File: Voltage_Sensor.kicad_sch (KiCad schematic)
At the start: 48 parts, among them IC1 AMC1350DWVR, IC2 AMC1350DWVR, U1 TLV9002QDRQ1, U2 TLV9002QDRQ1

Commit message: saving
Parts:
- removed C17: 1uF, Capacitor_SMD:C_0603_1608Metric_Pad1.08x0.95mm_HandSolder, symbol Device:C
- removed U2: TLV9002QDRQ1, Package_SO:SOIC-8_3.9x4.9mm_P1.27mm, symbol UTSVT-Misc:TLV9002QDRQ1
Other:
- note added: "Math for outp - outn difference Math for result"

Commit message: final schematic REV-A?
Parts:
- renumbered C2 to C1, C11 to C10, C12 to C11, C13 to C12, C14 to C13, C15 to C14, C16 to C15, C3 to C2, C4 to C3, C5 to C4, C6 to C5, C7 to C6, C8 to C7, C9 to C8, C10 to C9, R8 to R10, R9 to R11, R10 to R12, R11 to R13, R12 to R14, R13 to R15, R14 to R16, R15 to R17, R16 to R18, R17 to R19, R18 to R20, R19 to R21, R20 to R22, R21 to R23, R22 to R24, R23 to R25, R4 to R6, R5 to R7, R6 to R8, R7 to R9, TP9 to TP10, TP10 to TP11, TP3 to TP4, TP4 to TP5, TP5 to TP6, TP6 to TP7, TP7 to TP8, TP8 to TP9
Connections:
- net ISO_3V3 renamed ISO_5V
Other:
- moved on the sheet: C10, C11, C12, C4, C5, C6, C7, C8, C9, IC1, IC2, TP4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

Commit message: main isolation & motor isolation
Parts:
- R18, R21, R22, R23, R24, R25: footprint (none) -> Package_DIP:DIP-8_W7.62mm
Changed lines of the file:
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@@
 			)
 		)
-		(property "Footprint" ""
+		(property "Footprint" "Package_DIP:DIP-8_W7.62mm"
 			(at 217.17 113.538 90)
 			(hide yes)
@@
 			)
 		)
-		(property "Footprint" ""
+		(property "Footprint" "Package_DIP:DIP-8_W7.62mm"
 			(at 201.93 58.928 90)
 			(hide yes)
@@
 			)
 		)
-		(property "Footprint" ""
+		(property "Footprint" "Package_DIP:DIP-8_W7.62mm"
 			(at 184.15 58.928 90)
 			(hide yes)
@@
 			)
 		)
-		(property "Footprint" ""
+		(property "Footprint" "Package_DIP:DIP-8_W7.62mm"
 			(at 184.15 132.588 90)
 			(hide yes)
@@
 			)
 		)
-		(property "Footprint" ""
+		(property "Footprint" "Package_DIP:DIP-8_W7.62mm"
 			(at 217.17 39.878 90)
 			(hide yes)
@@
 			)
 		)
-		(property "Footprint" ""
+		(property "Footprint" "Package_DIP:DIP-8_W7.62mm"
 			(at 201.93 132.588 90)
 			(hide yes)

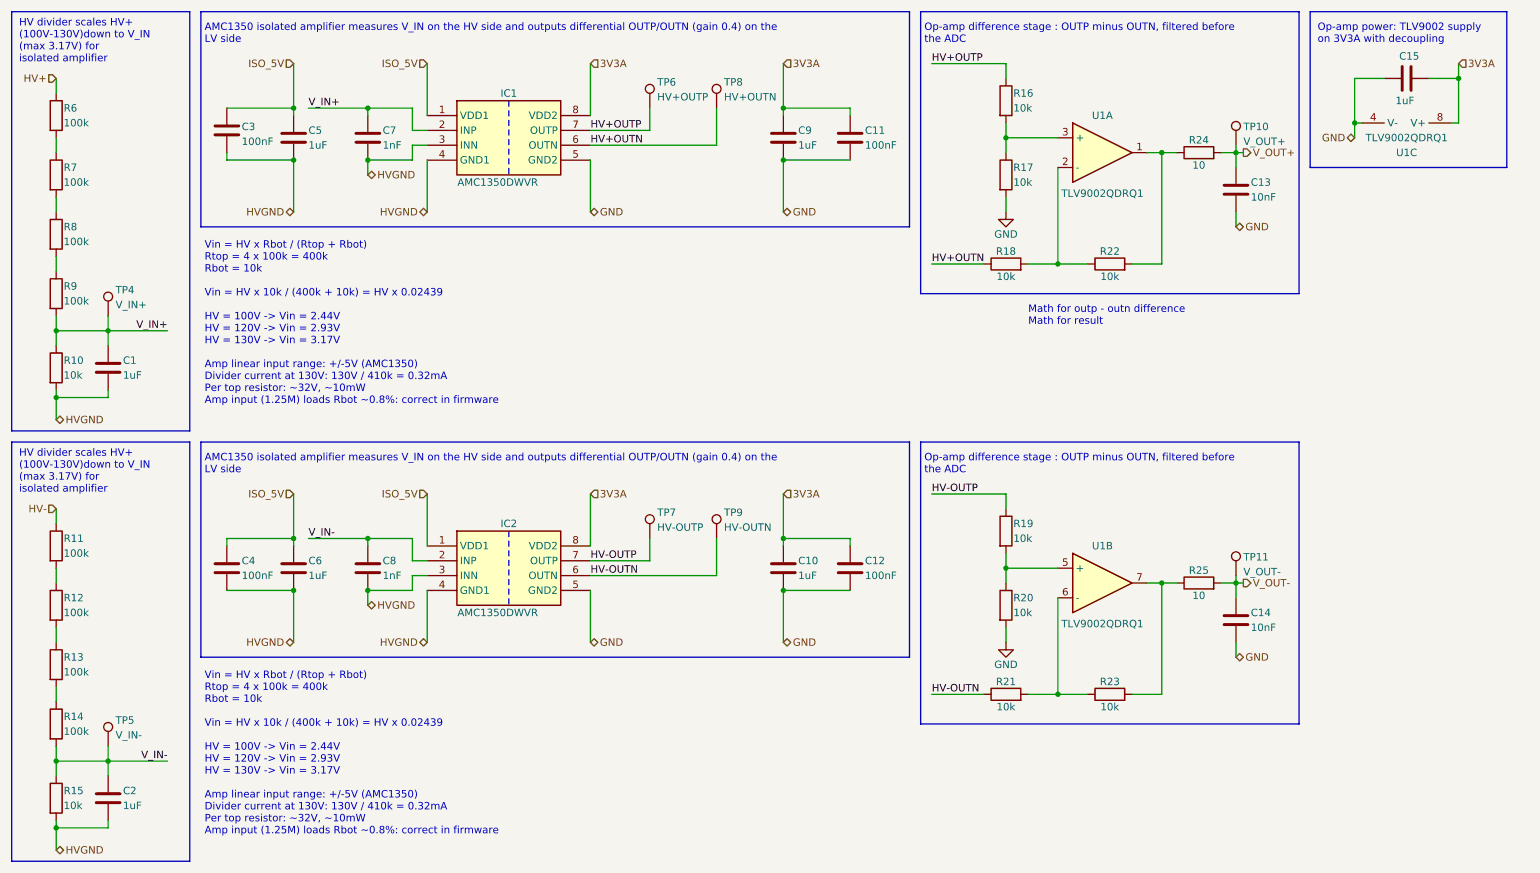
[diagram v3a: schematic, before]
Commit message: removed isolation for AMC3311
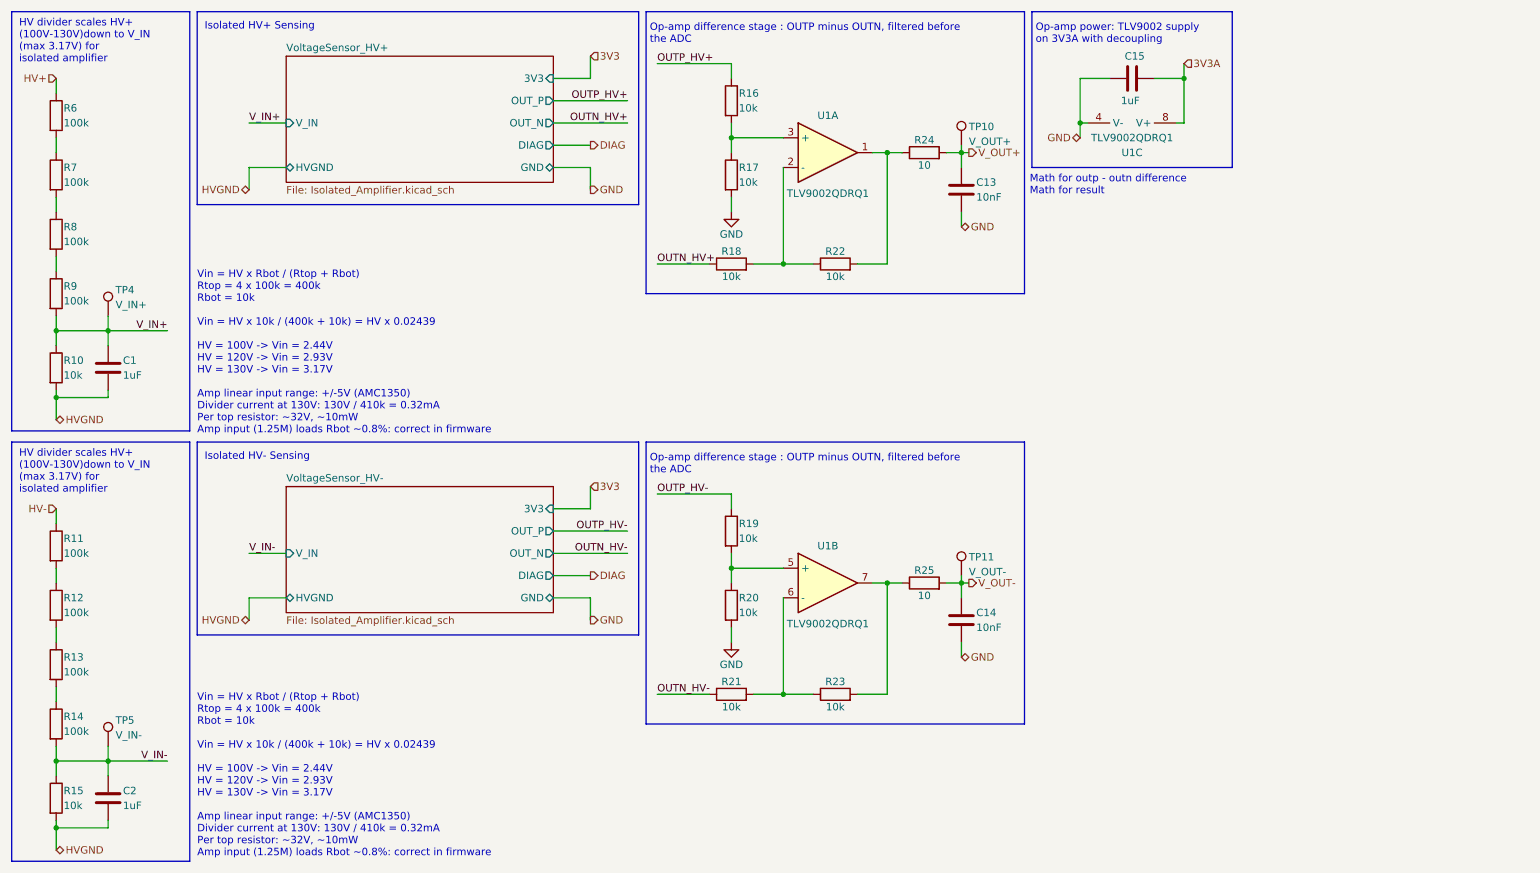
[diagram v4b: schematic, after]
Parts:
- removed C10, C5, C6, C9: 1uF, symbol Device:C
- removed C11, C12, C3, C4: 100nF, symbol Device:C
- removed C7, C8: 1nF, symbol Device:C
- removed IC1, IC2: AMC1350DWVR, ActivePrecharge-RevB:SOIC127P1150X280-8N, symbol AMC1350:AMC1350DWVR
- removed TP6: HV+OUTP, TestPoint:TestPoint_Loop_D1.80mm_Drill1.0mm_Beaded, symbol lhrs_misc:Multimeter_TP
- removed TP7: HV-OUTP, TestPoint:TestPoint_Loop_D1.80mm_Drill1.0mm_Beaded, symbol lhrs_misc:Multimeter_TP
- removed TP8: HV+OUTN, TestPoint:TestPoint_Loop_D1.80mm_Drill1.0mm_Beaded, symbol lhrs_misc:Multimeter_TP
- removed TP9: HV-OUTN, TestPoint:TestPoint_Loop_D1.80mm_Drill1.0mm_Beaded, symbol lhrs_misc:Multimeter_TP
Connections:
- net HV+OUTN renamed OUTN_HV+
- net HV+OUTP renamed OUTP_HV+
- net HV-OUTN renamed OUTN_HV-
- net HV-OUTP renamed OUTP_HV-
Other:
- added sheet VoltageSensor_HV+ (Isolated_Amplifier.kicad_sch)
- added sheet VoltageSensor_HV- (Isolated_Amplifier.kicad_sch)
- note added: "Isolated HV+ Sensing"
- note added: "Isolated HV- Sensing"
- note removed: "AMC1350 isolated amplifier measures V_IN on the HV side and outputs differential OUTP/OUTN (gain 0.4) on the LV side"
- moved on the sheet: C13, C14, C15, R16, R17, R18, R19, R20, R21, R22, R23, R24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

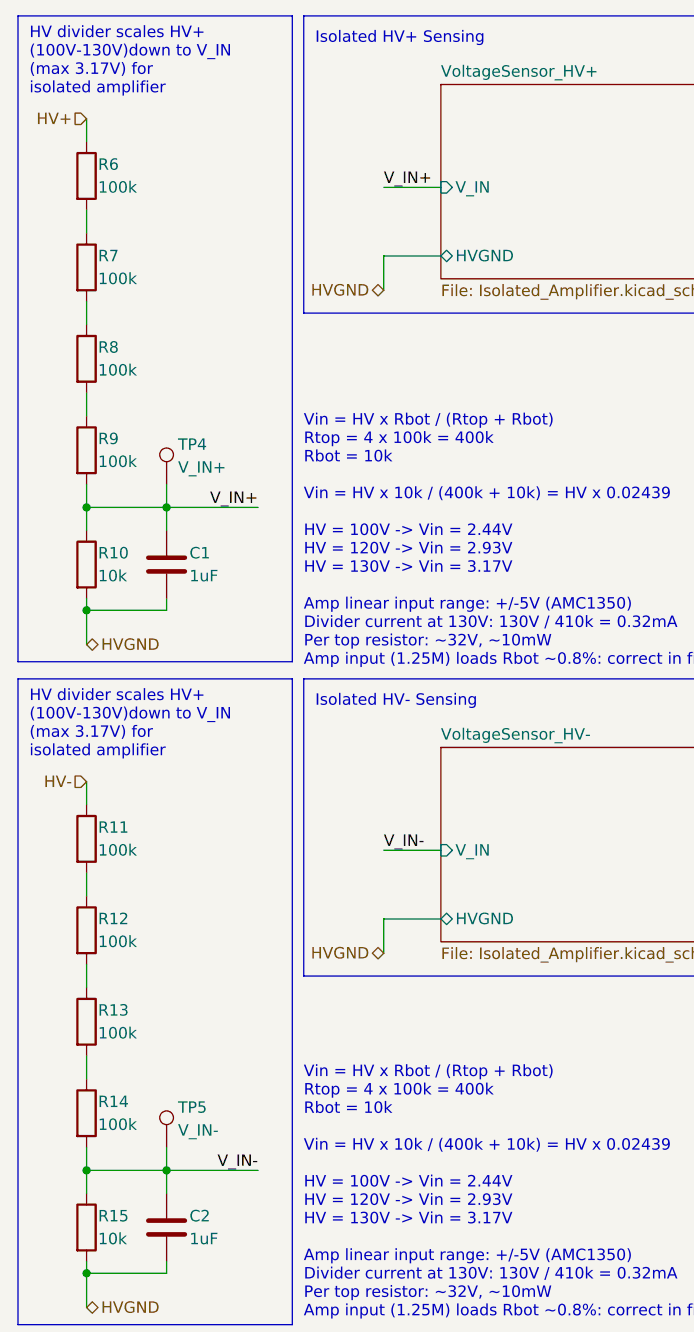
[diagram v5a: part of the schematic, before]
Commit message: added testpoints
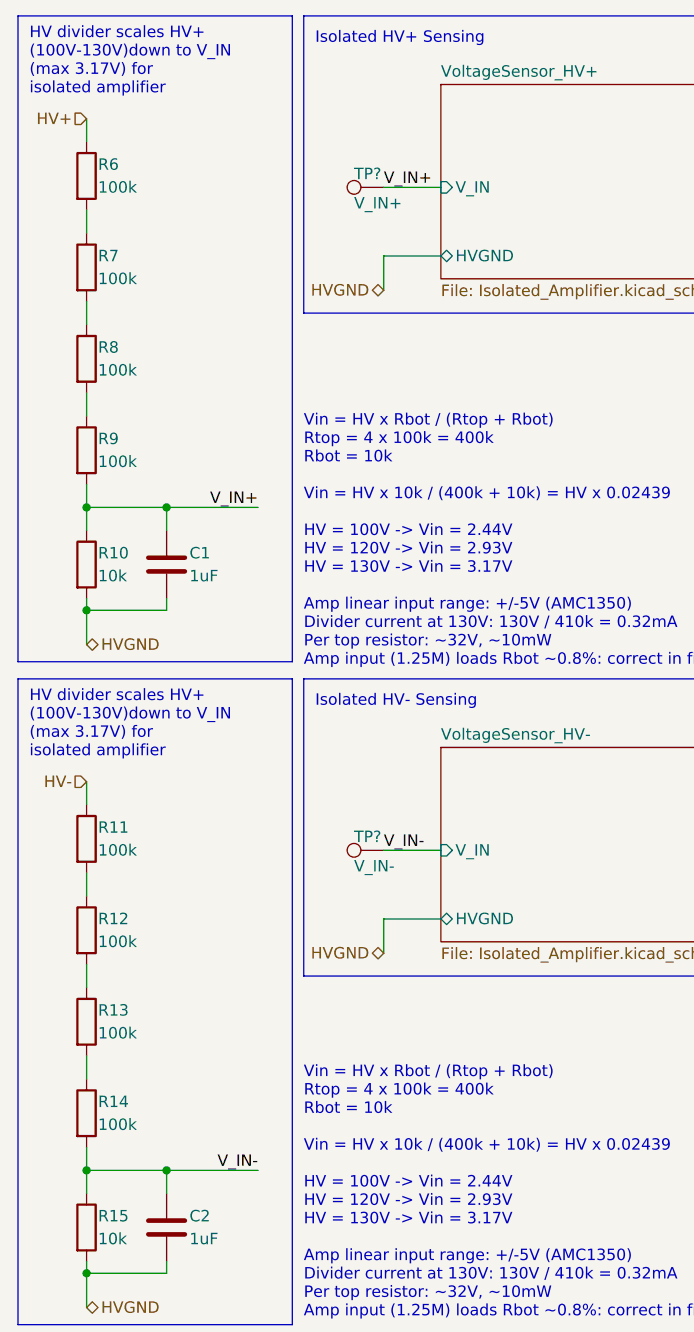
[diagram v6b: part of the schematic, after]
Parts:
- removed TP4: V_IN+, TestPoint:TestPoint_Loop_D1.80mm_Drill1.0mm_Beaded, symbol lhrs_misc:Multimeter_TP
- removed TP5: V_IN-, TestPoint:TestPoint_Loop_D1.80mm_Drill1.0mm_Beaded, symbol lhrs_misc:Multimeter_TP
- added TP?: V_IN+, TestPoint:TestPoint_Loop_D1.80mm_Drill1.0mm_Beaded, symbol lhrs_misc:Multimeter_TP
- added TP?: V_IN-, TestPoint:TestPoint_Loop_D1.80mm_Drill1.0mm_Beaded, symbol lhrs_misc:Multimeter_TP
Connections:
- net V_IN+: now also TP?.1
- net V_IN-: now also TP?.1
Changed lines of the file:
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@@
-	(wire
-		(pts
-			(xy 30.48 66.04) (xy 30.48 68.58)
-		)
-		(stroke
-			(width 0)
-			(type default)
-		)
-	)
 	(wire
 		(pts
@@
 		(pts
 			(xy 119.38 29.21) (xy 106.68 29.21)
-		)
-		(stroke
-			(width 0)
-			(type default)
-		)
-	)
-	(wire
-		(pts
-			(xy 30.48 139.7) (xy 30.48 142.24)
 		)
 		(stroke
@@
 			)
 			(justify left)
-		)
-	)
-	(symbol
-		(lib_id "lhrs_misc:Multimeter_TP")
-		(at 30.48 134.62 0)
-		(unit 1)
-		(body_style 1)
-		(exclude_from_sim no)
-		(in_bom yes)
-		(on_board yes)
-		(in_pos_files yes)
-		(dnp no)
-		(property "Reference" "TP5"
-			(at 31.75 135.255 0)
-			(show_name no)
-			(do_not_autoplace no)
-			(effects
-				(font
-					(size 1.27 1.27)
-				)
-				(justify left)
-			)
-		)
-		(property "Value" "V_IN-"
-			(at 31.75 137.795 0)
-			(show_name no)
-			(do_not_autoplace no)
-			(effects
-				(font
-					(size 1.27 1.27)
-				)
-				(justify left)
-			)
-		)
-		(property "Footprint" "TestPoint:TestPoint_Loop_D1.80mm_Drill1.0mm_Beaded"
-			(at 30.48 134.62 0)
-			(hide yes)
-			(show_name no)
-			(do_not_autoplace no)
-			(effects
-				(font
-					(size 1.27 1.27)
-				)
-			)
-		)
-		(property "Datasheet" ""
-			(at 30.48 134.62 0)
-			(hide yes)
-			(show_name no)
-			(do_not_autoplace no)
-			(effects
-				(font
-					(size 1.27 1.27)
-				)
-			)
-		)
-		(property "Description" ""
-			(at 30.48 134.62 0)
-			(hide yes)
-			(show_name no)
-			(do_not_autoplace no)
-			(effects
-				(font
-					(size 1.27 1.27)
-				)
-			)
-		)
-		(pin "1"
-		)
-		(instances
-			(project "PS-PrechargeBoard"
-				(path "/74d17fe6-68d4-4bd7-954a-e2bbb58b1f1e/6627985a-aef4-4302-9d05-a969136ea8f4"
-					(reference "TP5")
-					(unit 1)
-				)
-				(path "/74d17fe6-68d4-4bd7-954a-e2bbb58b1f1e/c9d052f0-39c4-441f-8d4e-0430a3425be4"
-					(reference "TP?")
-					(unit 1)
-				)
-			)
 		)
 	)
@@
 	)
 	(symbol
+		(lib_id "lhrs_misc:Multimeter_TP")
+		(at 49.53 33.02 90)
+		(unit 1)
+		(body_style 1)
+		(exclude_from_sim no)
+		(in_bom yes)
+		(on_board yes)
+		(in_pos_files yes)
+		(dnp no)
+		(property "Reference" "TP?"
+			(at 51.308 32.258 90)
+			(show_name no)
+			(do_not_autoplace no)
+			(effects
+				(font
+					(size 1.27 1.27)
+				)
+				(justify right top)
+			)
+		)
+		(property "Value" "V_IN+"
+			(at 51.308 34.036 90)
+			(show_name no)
+			(do_not_autoplace no)
+			(effects
+				(font
+					(size 1.27 1.27)
+				)
+				(justify right bottom)
+			)
+		)
+		(property "Footprint" "TestPoint:TestPoint_Loop_D1.80mm_Drill1.0mm_Beaded"
+			(at 49.53 33.02 0)
+			(hide yes)
+			(show_name no)
+			(do_not_autoplace no)
+			(effects
+				(font
+					(size 1.27 1.27)
+				)
+			)
+		)
+		(property "Datasheet" ""
+			(at 49.53 33.02 0)
+			(hide yes)
+			(show_name no)
+			(do_not_autoplace no)
+			(effects
+				(font
+					(size 1.27 1.27)
+				)
+			)
+		)
+		(property "Description" ""
+			(at 49.53 33.02 0)
+			(hide yes)
+			(show_name no)
+			(do_not_autoplace no)
+			(effects
+				(font
+					(size 1.27 1.27)
+				)
+			)
+		)
+		(pin "1"
+		)
+		(instances
+			(project "PS-PrechargeBoard"
+				(path "/74d17fe6-68d4-4bd7-954a-e2bbb58b1f1e/6627985a-aef4-4302-9d05-a969136ea8f4"
+					(reference "TP?")
+					(unit 1)
+				)
+				(path "/74d17fe6-68d4-4bd7-954a-e2bbb58b1f1e/c9d052f0-39c4-441f-8d4e-0430a3425be4"
+					(reference "TP?")
+					(unit 1)
+				)
+			)
+		)
+	)
+	(symbol
 		(lib_id "UTSVT-Misc:TLV9002QDRQ1")
 		(at 153.67 38.1 0)
@@
 	)
 	(symbol
-		(lib_id "lhrs_misc:Multimeter_TP")
-		(at 30.48 60.96 0)
-		(unit 1)
-		(body_style 1)
-		(exclude_from_sim no)
-		(in_bom yes)
-		(on_board yes)
-		(in_pos_files yes)
-		(dnp no)
-		(property "Reference" "TP4"
-			(at 31.75 61.595 0)
-			(show_name no)
-			(do_not_autoplace no)
-			(effects
-				(font
-					(size 1.27 1.27)
-				)
-				(justify left)
-			)
-		)
-		(property "Value" "V_IN+"
-			(at 31.75 64.135 0)
-			(show_name no)
-			(do_not_autoplace no)
-			(effects
-				(font
-					(size 1.27 1.27)
-				)
-				(justify left)
-			)
-		)
-		(property "Footprint" "TestPoint:TestPoint_Loop_D1.80mm_Drill1.0mm_Beaded"
-			(at 30.48 60.96 0)
-			(hide yes)
-			(show_name no)
-			(do_not_autoplace no)
-			(effects
-				(font
-					(size 1.27 1.27)
-				)
-			)
-		)
-		(property "Datasheet" ""
-			(at 30.48 60.96 0)
-			(hide yes)
-			(show_name no)
-			(do_not_autoplace no)
-			(effects
-				(font
-					(size 1.27 1.27)
-				)
-			)
-		)
-		(property "Description" ""
-			(at 30.48 60.96 0)
-			(hide yes)
-			(show_name no)
-			(do_not_autoplace no)
-			(effects
-				(font
-					(size 1.27 1.27)
-				)
-			)
-		)
-		(pin "1"
-		)
-		(instances
-			(project "PS-PrechargeBoard"
-				(path "/74d17fe6-68d4-4bd7-954a-e2bbb58b1f1e/6627985a-aef4-4302-9d05-a969136ea8f4"
-					(reference "TP4")
-					(unit 1)
-				)
-				(path "/74d17fe6-68d4-4bd7-954a-e2bbb58b1f1e/c9d052f0-39c4-441f-8d4e-0430a3425be4"
-					(reference "TP?")
-					(unit 1)
-				)
-			)
-		)
-	)
-	(symbol
 		(lib_id "Device:R")
 		(at 21.59 125.73 0)
@@
 					(unit 1)
 				)
+			)
+		)
+	)
+	(symbol
+		(lib_id "lhrs_misc:Multimeter_TP")
+		(at 49.53 106.68 90)
+		(unit 1)
+		(body_style 1)
+		(exclude_from_sim no)
+		(in_bom yes)
+		(on_board yes)
+		(in_pos_files yes)
+		(dnp no)
+		(property "Reference" "TP?"
+			(at 51.308 105.918 90)
+			(show_name no)
+			(do_not_autoplace no)
+			(effects
+				(font
+					(size 1.27 1.27)
+				)
+				(justify right top)
+			)
+		)
+		(property "Value" "V_IN-"
+			(at 51.308 107.696 90)
+			(show_name no)
+			(do_not_autoplace no)
+			(effects
+				(font
+					(size 1.27 1.27)
+				)
+				(justify right bottom)
+			)
+		)
+		(property "Footprint" "TestPoint:TestPoint_Loop_D1.80mm_Drill1.0mm_Beaded"
+			(at 49.53 106.68 0)
+			(hide yes)
+			(show_name no)
+			(do_not_autoplace no)
+			(effects
+				(font
+					(size 1.27 1.27)
+				)
+			)
+		)
+		(property "Datasheet" ""
+			(at 49.53 106.68 0)
+			(hide yes)
+			(show_name no)
+			(do_not_autoplace no)
+			(effects
+				(font
+					(size 1.27 1.27)
+				)
+			)
+		)
+		(property "Description" ""
+			(at 49.53 106.68 0)
+			(hide yes)
+			(show_name no)
+			(do_not_autoplace no)
+			(effects
+				(font
+					(size 1.27 1.27)
+				)
+			)
+		)
+		(pin "1"
+		)
+		(instances
+			(project "PS-PrechargeBoard"
+				(path "/74d17fe6-68d4-4bd7-954a-e2bbb58b1f1e/6627985a-aef4-4302-9d05-a969136ea8f4"
+					(reference "TP?")
+					(unit 1)
+				)
+				(path "/74d17fe6-68d4-4bd7-954a-e2bbb58b1f1e/c9d052f0-39c4-441f-8d4e-0430a3425be4"
+					(reference "TP?")
+					(unit 1)
+				)

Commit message: AGND
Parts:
- removed TP?: V_IN-, TestPoint:TestPoint_Loop_D1.80mm_Drill1.0mm_Beaded, symbol lhrs_misc:Multimeter_TP
- added TP?: V_IN-, TestPoint:TestPoint_Loop_D1.80mm_Drill1.0mm_Beaded, symbol lhrs_misc:Multimeter_TP
- gave numbers to parts that had none: 1
- renumbered C13 to C3, C14 to C4, C15 to C5, TP10 to TP15, TP11 to TP16
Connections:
- net V_IN-: now also TP?.1
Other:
- sheet VoltageSensor_HV+ ports: added AGND; removed GND
- sheet VoltageSensor_HV- ports: added AGND; removed GND

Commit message: rx/tx fixed on can_transceiver
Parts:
- gave numbers to parts that had none: 1
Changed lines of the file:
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@@
 		(in_pos_files yes)
 		(dnp no)
-		(property "Reference" "TP?"
+		(property "Reference" "TP14"
 			(at 52.07 105.918 90)
 			(show_name no)
@@
 			(project "PS-PrechargeBoard"
 				(path "/74d17fe6-68d4-4bd7-954a-e2bbb58b1f1e/6627985a-aef4-4302-9d05-a969136ea8f4"
-					(reference "TP?")
-					(unit 1)
-				)
-				(path "/74d17fe6-68d4-4bd7-954a-e2bbb58b1f1e/c9d052f0-39c4-441f-8d4e-0430a3425be4"
-					(reference "TP?")
+					(reference "TP14")
+					(unit 1)
+				)
+				(path "/74d17fe6-68d4-4bd7-954a-e2bbb58b1f1e/c9d052f0-39c4-441f-8d4e-0430a3425be4"
+					(reference "TP18")
 					(unit 1)
 				)
@@
 		(in_pos_files yes)
 		(dnp no)
-		(property "Reference" "#PWR026"
+		(property "Reference" "#PWR028"
 			(at 137.16 128.27 0)
 			(hide yes)
@@
 			(project "PS-PrechargeBoard"
 				(path "/74d17fe6-68d4-4bd7-954a-e2bbb58b1f1e/6627985a-aef4-4302-9d05-a969136ea8f4"
-					(reference "#PWR026")
-					(unit 1)
-				)
-				(path "/74d17fe6-68d4-4bd7-954a-e2bbb58b1f1e/c9d052f0-39c4-441f-8d4e-0430a3425be4"
 					(reference "#PWR028")
+					(unit 1)
+				)
+				(path "/74d17fe6-68d4-4bd7-954a-e2bbb58b1f1e/c9d052f0-39c4-441f-8d4e-0430a3425be4"
+					(reference "#PWR030")
 					(unit 1)
 				)
@@
 		(in_pos_files yes)
 		(dnp no)
-		(property "Reference" "#PWR025"
+		(property "Reference" "#PWR027"
 			(at 137.16 54.61 0)
 			(hide yes)
@@
 			(project "PS-PrechargeBoard"
 				(path "/74d17fe6-68d4-4bd7-954a-e2bbb58b1f1e/6627985a-aef4-4302-9d05-a969136ea8f4"
-					(reference "#PWR025")
-					(unit 1)
-				)
-				(path "/74d17fe6-68d4-4bd7-954a-e2bbb58b1f1e/c9d052f0-39c4-441f-8d4e-0430a3425be4"
 					(reference "#PWR027")
 					(unit 1)
 				)
+				(path "/74d17fe6-68d4-4bd7-954a-e2bbb58b1f1e/c9d052f0-39c4-441f-8d4e-0430a3425be4"
+					(reference "#PWR029")
+					(unit 1)
+				)
